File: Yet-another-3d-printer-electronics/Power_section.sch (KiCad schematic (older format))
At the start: 26 parts, among them J2 DG638, J3 TEST_3.3V, J4 TEST_5V, J5 TEST_12V, U7 AP1501, U8 AP1501, U9 AP1501

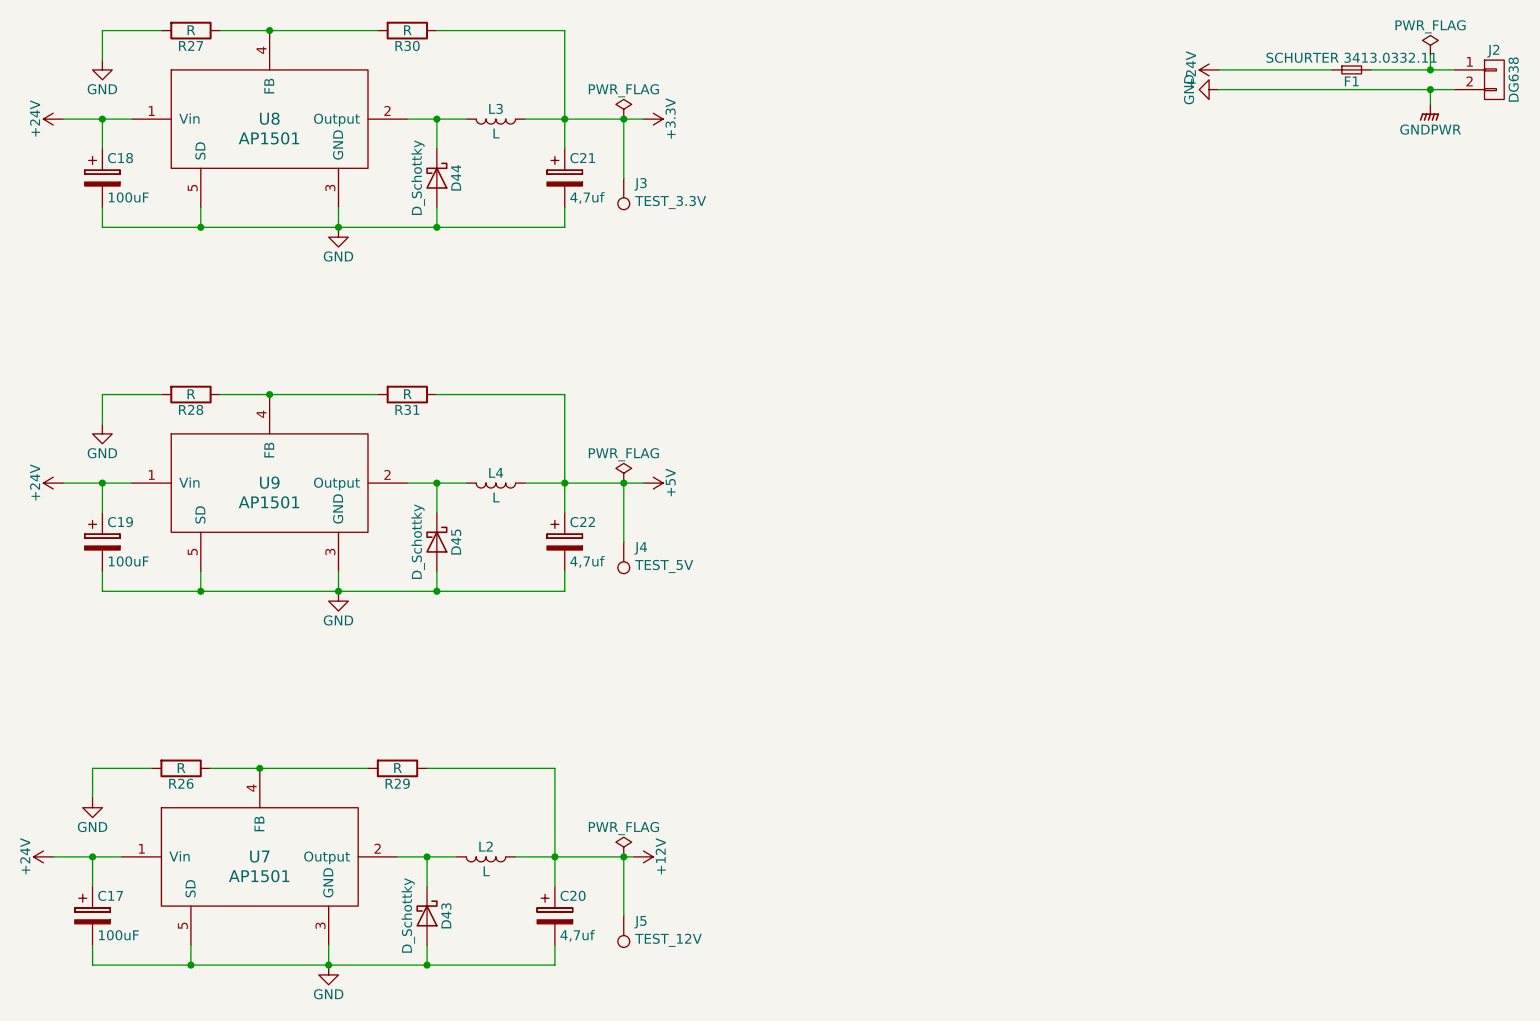
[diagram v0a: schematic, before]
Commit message: Add HPI1260, HPI0630 footprints, add estimated value for choke smds
Signed-off-by: Mateusz Krawczuk <mat.krawczuk@gmail.com>
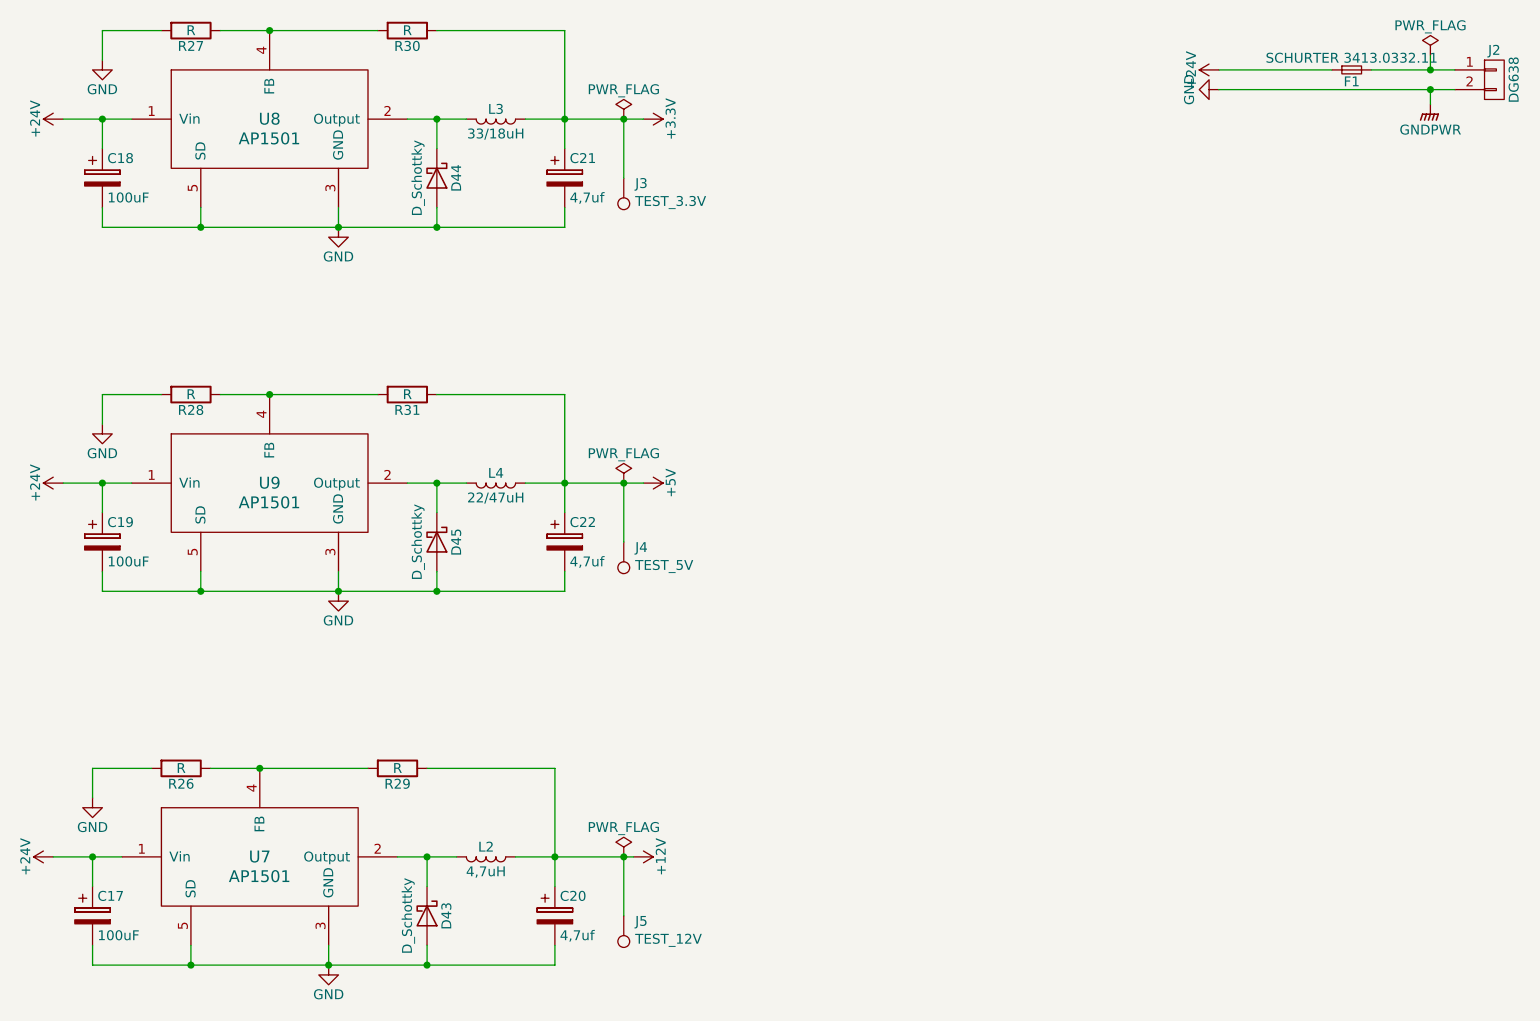
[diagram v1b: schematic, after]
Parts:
- L2: value L -> 4,7uH; footprint (none) -> Yet-another-3d-printer-electronics:HP1260
- L3: value L -> 33/18uH; footprint (none) -> Yet-another-3d-printer-electronics:HP1260
- L4: value L -> 22/47uH; footprint (none) -> Yet-another-3d-printer-electronics:HP1260
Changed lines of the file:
@@
 P 4350 1900
 F 0 "L3" V 4300 1900 50  0000 C CNN
-F 1 "L" V 4425 1900 50  0000 C CNN
-F 2 "" H 4350 1900 50  0001 C CNN
+F 1 "33/18uH" V 4425 1900 50  0000 C CNN
+F 2 "Yet-another-3d-printer-electronics:HP1260" H 4350 1900 50  0001 C CNN
 F 3 "" H 4350 1900 50  0001 C CNN
 	1    4350 1900
@@
 P 4350 3750
 F 0 "L4" V 4300 3750 50  0000 C CNN
-F 1 "L" V 4425 3750 50  0000 C CNN
-F 2 "" H 4350 3750 50  0001 C CNN
-F 3 "" H 4350 3750 50  0001 C CNN
+F 1 "22/47uH" V 4425 3750 50  0000 C CNN
+F 2 "Yet-another-3d-printer-electronics:HP1260" H 4350 3750 50  0001 C CNN
+F 3 "HPI1260-220" H 4350 3750 50  0001 C CNN
 	1    4350 3750
 	0    1    1    0
@@
 P 4300 5650
 F 0 "L2" V 4250 5650 50  0000 C CNN
-F 1 "L" V 4375 5650 50  0000 C CNN
-F 2 "" H 4300 5650 50  0001 C CNN
-F 3 "" H 4300 5650 50  0001 C CNN
+F 1 "4,7uH" V 4375 5650 50  0000 C CNN
+F 2 "Yet-another-3d-printer-electronics:HP1260" H 4300 5650 50  0001 C CNN
+F 3 "HPI0630-4R7" H 4300 5650 50  0001 C CNN
 	1    4300 5650
 	0    1    1    0

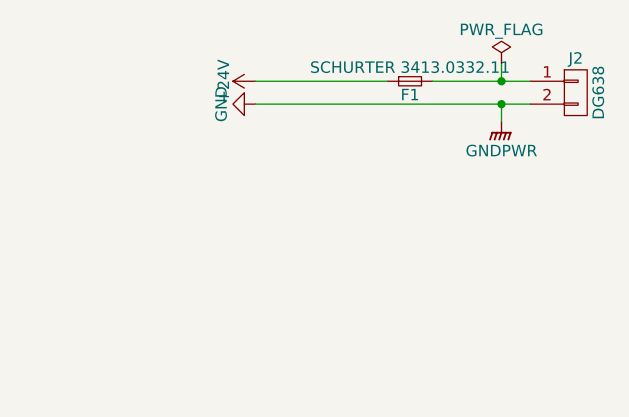
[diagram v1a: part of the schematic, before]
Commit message: Choose footprint for fuses and add TVS to power source connection
Signed-off-by: Mateusz Krawczuk <mat.krawczuk@gmail.com>
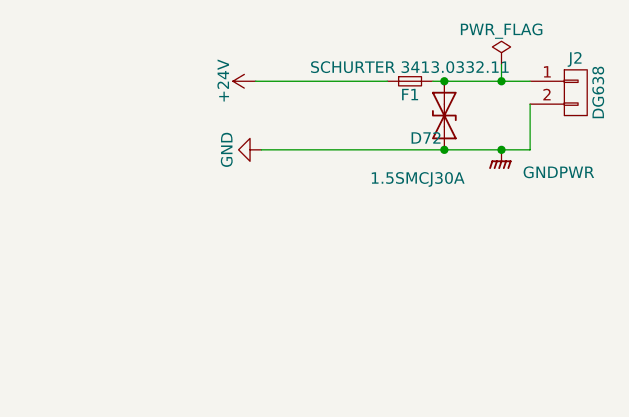
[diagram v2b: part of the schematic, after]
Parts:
- added D72: 1.5SMCJ30A, Yet-another-3d-printer-electronics:DO-214AC(SMA), symbol D_TVS
- F1: footprint (none) -> Fuse_Holders_and_Fuses:Fuse_SMD1206_HandSoldering
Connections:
- net GND: now also D72.2 (A2)
- net at F1.2, J2.1 (P1): now also D72.1 (A1)
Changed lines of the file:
@@
 L GND #PWR097
 U 1 1 58FF7FE9
-P 8025 1750
-F 0 "#PWR097" H 8025 1500 50  0001 C CNN
-F 1 "GND" H 8025 1600 50  0000 C CNN
-F 2 "" H 8025 1750 50  0001 C CNN
-F 3 "" H 8025 1750 50  0001 C CNN
-	1    8025 1750
+P 8050 1950
+F 0 "#PWR097" H 8050 1700 50  0001 C CNN
+F 1 "GND" H 8050 1800 50  0000 C CNN
+F 2 "" H 8050 1950 50  0001 C CNN
+F 3 "" H 8050 1950 50  0001 C CNN
+	1    8050 1950
 	0    1    1    0
 $EndComp
-Wire Wire Line
-	8025 1750 9225 1750
 $Comp
 L GNDPWR #PWR098
 U 1 1 58FF8089
-P 9100 1825
-F 0 "#PWR098" H 9100 1625 50  0001 C CNN
-F 1 "GNDPWR" H 9100 1695 50  0000 C CNN
-F 2 "" H 9100 1775 50  0001 C CNN
-F 3 "" H 9100 1775 50  0001 C CNN
-	1    9100 1825
+P 9100 1950
+F 0 "#PWR098" H 9100 1750 50  0001 C CNN
+F 1 "GNDPWR" H 9350 1850 50  0000 C CNN
+F 2 "" H 9100 1900 50  0001 C CNN
+F 3 "" H 9100 1900 50  0001 C CNN
+	1    9100 1950
 	1    0    0    -1
 $EndComp
-Wire Wire Line
-	9100 1825 9100 1750
-Connection ~ 9100 1750
 $Comp
 L PWR_FLAG #FLG099
@@
 F 0 "F1" H 8700 1590 50  0000 C CNN
 F 1 "SCHURTER 3413.0332.11" H 8700 1710 50  0000 C CNN
-F 2 "" H 8700 1650 50  0001 C CNN
+F 2 "Fuse_Holders_and_Fuses:Fuse_SMD1206_HandSoldering" H 8700 1650 50  0001 C CNN
 F 3 "" H 8700 1650 50  0001 C CNN
 	1    8700 1650
@@
 	-1   0    0    1
 $EndComp
+$Comp
+L D_TVS D72
+U 1 1 598762F1
+P 8850 1800
+F 0 "D72" V 8950 1650 50  0000 L CNN
+F 1 "1.5SMCJ30A" V 9125 1475 50  0000 L CNN
+F 2 "Yet-another-3d-printer-electronics:DO-214AC(SMA)" H 8850 1800 50  0001 C CNN
+F 3 "" H 8850 1800 50  0001 C CNN
+	1    8850 1800
+	0    1    1    0
+$EndComp
+Wire Wire Line
+	8050 1950 9225 1950
+Connection ~ 8850 1950
+Wire Wire Line
+	9225 1950 9225 1750
+Connection ~ 9100 1950
+Connection ~ 8850 1650
 $EndSCHEMATC
